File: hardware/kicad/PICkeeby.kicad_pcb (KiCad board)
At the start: 4 copper layers, 85.7 x 55.9 mm, 35 parts, among them J1 PS/2 Connector, J2 PS/2 Connector, J3 MODE_SELECT, J4 Host Interface, J5 Conn_PIC_ICSP_ICD, J6 PS/2 Header, J7 PS/2 Header, U1 PIC16F18344-P, U2 74HCT574, U3 74HCT373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

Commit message: v2
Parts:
- removed D5: LED, LED_THT:LED_D3.0mm_FlatTop
- removed R7: 470R, Resistor_THT:R_Axial_DIN0207_L6.3mm_D2.5mm_P10.16mm_Horizontal
- added x1: PinHeader_1x02_P2.54mm_Vertical, Connector_PinHeader_2.54mm:PinHeader_1x02_P2.54mm_Vertical, B.Cu at (10.2, 17.9)
- added x2: PinHeader_1x02_P2.54mm_Vertical, Connector_PinHeader_2.54mm:PinHeader_1x02_P2.54mm_Vertical, B.Cu at (10.1, 43.3)
- added x3: PinHeader_1x02_P2.54mm_Vertical, Connector_PinHeader_2.54mm:PinHeader_1x02_P2.54mm_Vertical, B.Cu at (84.2, 17.9)
- added x4: PinHeader_1x02_P2.54mm_Vertical, Connector_PinHeader_2.54mm:PinHeader_1x02_P2.54mm_Vertical, B.Cu at (84.2, 43.3)
- C1, C2, C3, C4, C5, C6, C7, C8: footprint Capacitor_THT:C_Disc_D6.0mm_W2.5mm_P5.00mm -> Capacitor_SMD:C_0805_2012Metric_Pad1.18x1.45mm_HandSolder
- R1, R10, R11, R2, R3, R4, R5, R6, R8, R9: footprint Resistor_THT:R_Axial_DIN0207_L6.3mm_D2.5mm_P10.16mm_Horizontal -> Resistor_SMD:R_0805_2012Metric_Pad1.20x1.40mm_HandSolder
- U2, U3: footprint Package_DIP:DIP-20_W7.62mm_Socket_LongPads -> Package_SO:SOIC-20W_7.5x12.8mm_P1.27mm
- moved J5 180.9 mm to (10.2, 26.7)
- moved R1 173.5 mm to (11.2, 23.7)
- moved J6 173.5 mm to (28.1, 9.04), turned to 0 degrees
- moved J1 166.8 mm to (39.1, 11.5), turned to 180 degrees
- moved R3 163.4 mm to (25.2, 10.5), turned to 90 degrees
- moved J2 160.5 mm to (55.2, 11.5), turned to 180 degrees
- moved R2 157.5 mm to (23.2, 10.5), turned to -90 degrees
- moved R8 155.8 mm to (33.6, 21.7), turned to 180 degrees
- moved D3 155.8 mm to (33.6, 26.7)
- moved R9 152.1 mm to (42.6, 21.7), turned to 180 degrees
- moved U1 148.5 mm to (24.8, 43.4), turned to 180 degrees
- moved R10 148.4 mm to (51.7, 21.8), turned to 180 degrees
- moved J7 145.3 mm to (66.1, 8.99), turned to 0 degrees
- moved D1 141.6 mm to (42.6, 26.7)
- moved D2 138.1 mm to (51.7, 26.7)
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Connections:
- J1 pad S1: GND -> (no net)
- J1 pad S2: GND -> (no net)
- J1 pad S3: GND -> (no net)
- J2 pad S1: GND -> (no net)
- J2 pad S2: GND -> (no net)
- J2 pad S3: GND -> (no net)
- J4 pad 2: /HDATA0 -> /HDATA7
- J4 pad 3: /HDATA1 -> /HDATA6
- J4 pad 4: /HDATA2 -> /HDATA5
- J4 pad 5: /HDATA3 -> /HDATA4
- J4 pad 6: /HDATA4 -> /HDATA3
- J4 pad 7: /HDATA5 -> /HDATA2
- J4 pad 8: /HDATA6 -> /HDATA1
- J4 pad 9: /HDATA7 -> /HDATA0
- J5 pad 1: VPP -> A0
- R1 pad 2: VPP -> A0
- R10 pad 1: Net-(D5-A) -> Net-(D2-A)
- R6 pad 1: Net-(D1-A) -> Net-(D4-A)
- R8 pad 2: Net-(R8-Pad2) -> LED_RX
- R9 pad 1: Net-(D4-A) -> Net-(D1-A)
- U1 pad 4: VPP -> A0
- U2 pad 1: unconnected-(U2-OE-Pad1) -> ~{RD_DATA}
- U4 pad 16: Net-(R8-Pad2) -> LED_RX
- U4 pad 21: Net-(R7-Pad2) -> /HDATA5
- U4 pad 8: GND -> ~{AUX}
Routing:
- net +5V: track 42.1 -> 222.5 mm, vias 3 -> 0
- net LED_RX: track 0.00 -> 115.4 mm, vias 0 -> 1
- net ~{AUX}: track 0.00 -> 60.6 mm
- net Net-(R8-Pad2): track 55.0 -> 0.00 mm, vias 1 -> 0
- net ~{RD_DATA}: track 0.00 -> 45.5 mm, vias 0 -> 1
- net SIG2: track 69.6 -> 24.3 mm, vias 2 -> 0
- net PS2_DATA1: track 77.5 -> 37.0 mm, vias 1 -> 0
- net SIG1: track 66.3 -> 27.4 mm
- net Net-(R7-Pad2): track 38.5 -> 0.00 mm, vias 1 -> 0
- net VPP: track 34.5 -> 0.00 mm, vias 1 -> 0
- net ~{CS}: track 53.4 -> 22.2 mm, vias 1 -> 0
- net /HDATA2: track 76.8 -> 46.4 mm
- net /IDATA3: track 58.5 -> 29.8 mm, vias 4 -> 0
- net ~{IRQ}: track 45.0 -> 17.1 mm, vias 1 -> 0
- net A0: track 93.1 -> 119.5 mm
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- added copper zone on B.Cu, net GND
- removed copper zone on In2.Cu, net +5V
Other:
- board size 85.7 x 55.9 mm -> 78.4 x 39.5 mm
- board text added: "PS/2 Interface"
- board text added: "Tom Keller 2026 tom@tompkel.net"
- board text removed: "1"
- board text removed: "2"
- board text removed: "5"
- board text removed: "C"
- board text removed: "CS"
- board text removed: "D"
- board text removed: "G"
- board text removed: "ICSP"
- board text removed: "PS/2"
- board text removed: "PS/2 Keyboard Interface"

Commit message: v2
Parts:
- removed C6: 10nf, Capacitor_SMD:C_0805_2012Metric_Pad1.18x1.45mm_HandSolder
- removed C7: 100nF, Capacitor_SMD:C_0805_2012Metric_Pad1.18x1.45mm_HandSolder
- removed C8: 10nF, Capacitor_SMD:C_0805_2012Metric_Pad1.18x1.45mm_HandSolder
- removed R10: 470R, Resistor_SMD:R_0805_2012Metric_Pad1.20x1.40mm_HandSolder
- removed R11: 10K, Resistor_SMD:R_0805_2012Metric_Pad1.20x1.40mm_HandSolder
- removed U4: ATF22V10C-10PC, Package_DIP:DIP-24_W7.62mm_Socket_LongPads
- added R7: 300Ω, Resistor_SMD:R_0805_2012Metric_Pad1.20x1.40mm_HandSolder, F.Cu at (39.3, 23.3)
- added U5: 74AHCT1G14, Package_TO_SOT_SMD:SOT-23-5_HandSoldering, F.Cu at (85.5, 75.3)
- C1, C3, C5: value 100nF -> 1µF
- C2, C4: value 10nf -> 1µF
- R1: value 100K -> 4K7
- R5: value 4K7 -> 300Ω
- R6, R8: value 470R -> 300Ω
- R9: value 470R -> 10K
- U2: value 74HCT574 -> 74AHCT574
- U3: value 74HCT373 -> 74AHCT373
- moved C2 66.2 mm to (68.6, 74.3), turned to 90 degrees
- moved C1 62.1 mm to (28.4, 43.4)
- moved C5 59.5 mm to (85.4, 71.8)
- moved R3 56.7 mm to (81.9, 9.07)
- moved U3 53.0 mm to (76.6, 70.3), turned to -90 degrees
- moved C3 52.1 mm to (85.5, 69.7), turned to 0 degrees
- moved R9 42.1 mm to (84.7, 22.9), turned to -90 degrees
- moved U2 35.8 mm to (60.6, 70.3), turned to -90 degrees
- moved C4 28.5 mm to (77.8, 8.72), turned to 180 degrees
- moved D4 27.5 mm to (33.6, 21.4), turned to -90 degrees
- moved R5 19.2 mm to (57.3, 23.3), turned to 90 degrees
- moved R1 18.8 mm to (23.2, 9.10), turned to -90 degrees
- moved D1 18.8 mm to (60.7, 21.4), turned to -90 degrees
- moved J3 15.0 mm to (81.7, 28.9)
- moved R6 12.4 mm to (48.3, 23.3), turned to 90 degrees
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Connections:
- D1 pad 1: GND -> ~{CS}
- J4 pad 1: +5V -> /HDATA7
- J4 pad 10: A0 -> SIG1
- J4 pad 11: SIG1 -> SIG2
- J4 pad 13: SIG2 -> ~{IRQ}
- J4 pad 14: ~{IRQ} -> +5V
- J4 pad 2: /HDATA7 -> /HDATA6
- J4 pad 3: /HDATA6 -> /HDATA5
- J4 pad 4: /HDATA5 -> /HDATA4
- J4 pad 5: /HDATA4 -> /HDATA3
- J4 pad 6: /HDATA3 -> /HDATA2
- J4 pad 7: /HDATA2 -> /HDATA1
- J4 pad 8: /HDATA1 -> /HDATA0
- J4 pad 9: /HDATA0 -> A0
- J5 pad 1: A0 -> VPP
- R1 pad 2: A0 -> PS2_CLK1
- R2 pad 1: +5V -> PS2_DATA1
- R2 pad 2: PS2_CLK1 -> +5V
- R3 pad 1: PS2_DATA1 -> +5V
- R3 pad 2: +5V -> PS2_CLK2
- R4 pad 1: +5V -> PS2_DATA2
- R4 pad 2: PS2_CLK2 -> +5V
- R5 pad 1: PS2_DATA2 -> Net-(D1-A)
- R6 pad 1: Net-(D4-A) -> Net-(D2-A)
- R8 pad 1: Net-(D3-A) -> Net-(D4-A)
- R8 pad 2: LED_RX -> Net-(R8-Pad2)
- R9 pad 1: Net-(D1-A) -> +5V
- R9 pad 2: Net-(R9-Pad2) -> Net-(J3-Pin_3)
- U1 pad 3: LED_RX -> IBF
- U1 pad 4: A0 -> A0_REG
- U3 pad 12: /HDATA4 -> /IDATA4
- U3 pad 13: /IDATA4 -> /HDATA4
- U3 pad 14: /IDATA5 -> /HDATA5
- U3 pad 15: /HDATA5 -> /IDATA5
- U3 pad 16: /HDATA6 -> /IDATA6
- U3 pad 17: /IDATA6 -> /HDATA6
- U3 pad 18: /IDATA7 -> /HDATA7
- U3 pad 19: /HDATA7 -> /IDATA7
- U3 pad 2: /HDATA0 -> /IDATA0
- U3 pad 3: /IDATA0 -> /HDATA0
- U3 pad 4: /IDATA1 -> /HDATA1
- U3 pad 5: /HDATA1 -> /IDATA1
- U3 pad 6: /HDATA2 -> /IDATA2
- U3 pad 7: /IDATA2 -> /HDATA2
- U3 pad 8: /IDATA3 -> /HDATA3
- U3 pad 9: /HDATA3 -> /IDATA3
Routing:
- net +5V: track 222.5 -> 0.00 mm
- net A0: track 119.5 -> 0.00 mm, vias 4 -> 0
- net LED_RX: track 115.4 -> 0.00 mm, vias 1 -> 0
- net CLK_OUT: track 109.1 -> 0.00 mm, vias 4 -> 0
- net ~{IBF_CLR}: track 69.8 -> 0.00 mm
- net /HDATA5: track 68.5 -> 0.00 mm, vias 2 -> 0
- net PS2_CLK2: track 65.9 -> 0.00 mm, vias 1 -> 0
- net /HDATA1: track 64.5 -> 0.00 mm, vias 2 -> 0
- net ~{AUX}: track 60.6 -> 0.00 mm
- net /IDATA5: track 59.7 -> 0.00 mm
- net Net-(R9-Pad2): track 57.4 -> 0.00 mm, vias 3 -> 0
- net /HDATA0: track 57.1 -> 0.00 mm, vias 2 -> 0
- net /HDATA6: track 56.7 -> 0.00 mm, vias 2 -> 0
- net LE_IN: track 53.8 -> 0.00 mm, vias 1 -> 0
- net /HDATA4: track 52.8 -> 0.00 mm, vias 2 -> 0
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
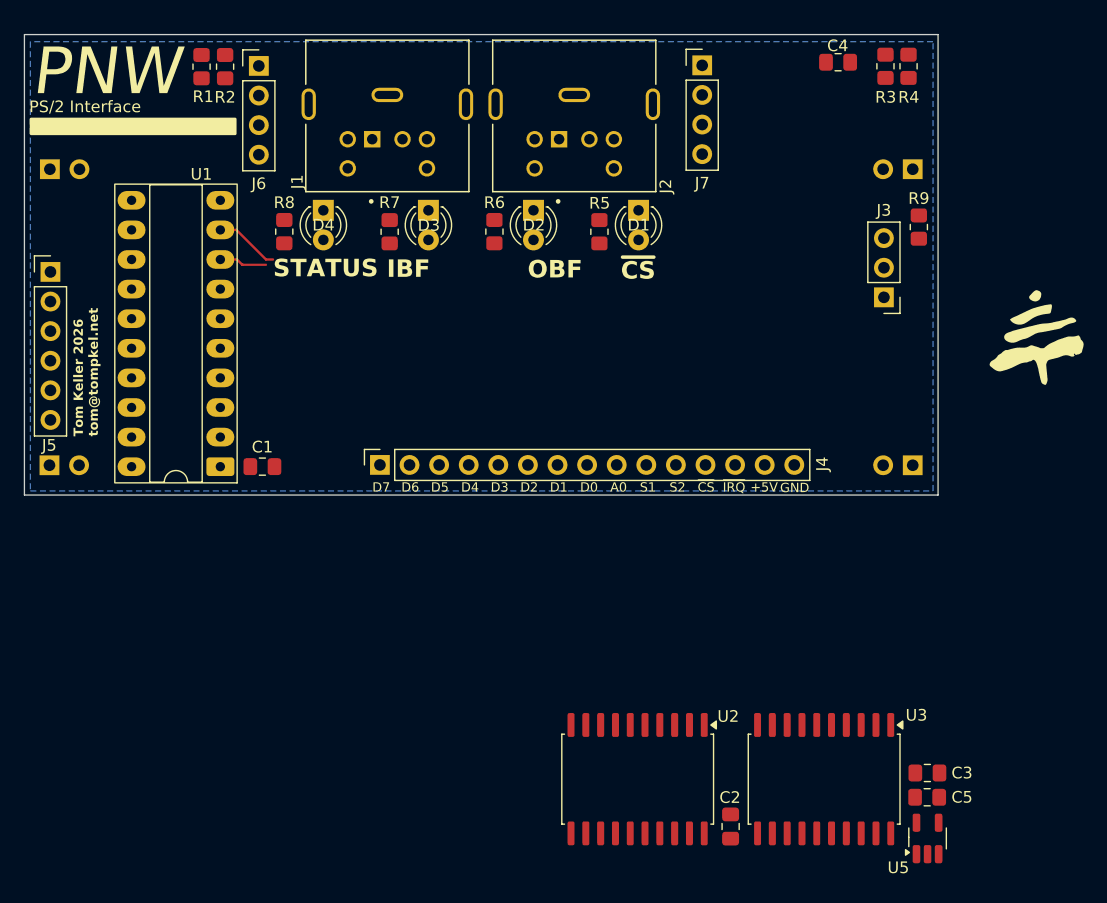
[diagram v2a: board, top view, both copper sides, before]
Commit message: GAL async reset for IBF clear, doc fixes, linting
- PLD: Add AR product term for async IBF/A0_REG clear (fixes Z80 deadlock)
- Firmware: Fix LATA init (OE_INB high at startup), simplify IBF clear
- Firmware: Move IDATA remap functions from pins.h to host.c
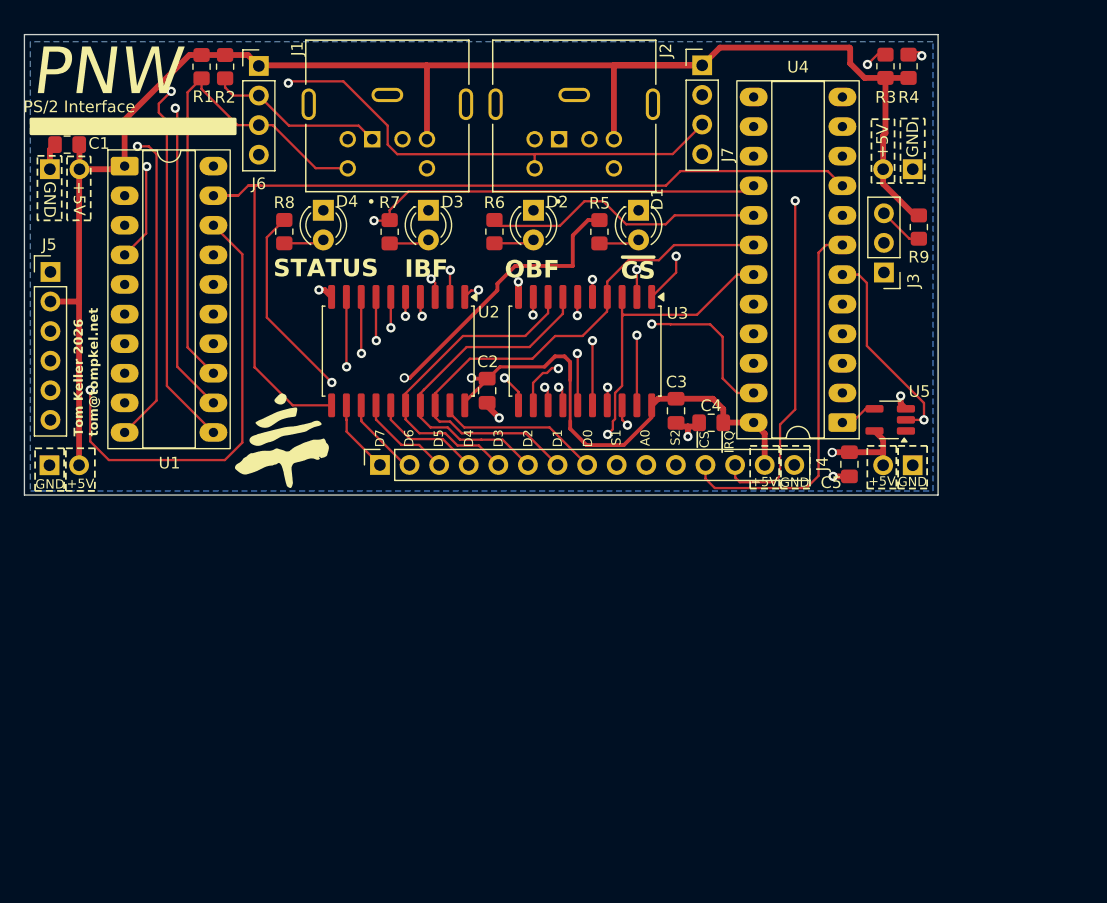
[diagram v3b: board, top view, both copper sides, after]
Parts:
- added U4: ATF22V10C-10PC, Package_DIP:DIP-24_W7.62mm_Socket_LongPads, F.Cu at (78.2, 39.6)
- moved C2 42.8 mm to (47.7, 36.9), turned to -90 degrees
- moved U2 42.1 mm to (40.1, 33.5)
- moved U3 42.1 mm to (56.1, 33.5)
- moved U5 36.1 mm to (82.3, 39.4), turned to 180 degrees
- moved C3 35.3 mm to (66.9, 39.7), turned to 180 degrees
- moved C4 33.0 mm to (63.9, 38.6), turned to -90 degrees
- moved C1 32.3 mm to (11.6, 15.8), turned to 180 degrees
- moved C5 29.3 mm to (78.8, 43.2), turned to -90 degrees
- moved U1 27.1 mm to (16.6, 17.6), turned to 0 degrees
- moved J3 2.13 mm to (81.7, 26.8)
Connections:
- J4 pad 10: SIG1 -> A0
- J4 pad 9: A0 -> SIG1
- U1 pad 14: /IDATA2 -> /IDATA5
- U1 pad 15: /IDATA1 -> /IDATA3
- U1 pad 16: /IDATA0 -> /IDATA1
- U1 pad 5: /IDATA5 -> /IDATA0
- U1 pad 6: /IDATA4 -> /IDATA2
- U1 pad 7: /IDATA3 -> /IDATA4
- U3 pad 12: /IDATA4 -> /IDATA7
- U3 pad 13: /HDATA4 -> /HDATA7
- U3 pad 14: /HDATA5 -> /HDATA6
- U3 pad 15: /IDATA5 -> /IDATA6
- U3 pad 16: /IDATA6 -> /IDATA5
- U3 pad 17: /HDATA6 -> /HDATA5
- U3 pad 18: /HDATA7 -> /HDATA4
- U3 pad 19: /IDATA7 -> /IDATA4
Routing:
- net +5V: track 0.00 -> 265.3 mm, vias 0 -> 3
- net CLK_OUT: track 0.00 -> 108.0 mm
- net PS2_CLK2: track 0.00 -> 105.9 mm, vias 0 -> 3
- net PS2_DATA2: track 0.00 -> 101.4 mm, vias 0 -> 2
- net ~{OE_IN}: track 0.00 -> 90.8 mm, vias 0 -> 2
- net Net-(R8-Pad2): track 0.00 -> 65.3 mm, vias 0 -> 1
- net A0_REG: track 0.00 -> 65.2 mm, vias 0 -> 1
- net ~{AUX}: track 0.00 -> 63.2 mm
- net IBF: track 0.00 -> 56.2 mm, vias 0 -> 1
- net ~{IBF_CLR}: track 0.00 -> 55.1 mm
- net /IDATA4: track 0.00 -> 53.5 mm, vias 0 -> 2
- net ~{CS}: track 0.00 -> 51.8 mm
- net PS2_DATA1: track 0.00 -> 49.7 mm, vias 0 -> 1
- net /IDATA0: track 0.00 -> 49.4 mm, vias 0 -> 2
- net /HDATA1: track 0.00 -> 48.3 mm
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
